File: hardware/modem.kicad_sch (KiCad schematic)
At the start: 30 parts, among them J11 PRPC001DAAN-RC, Q3 IRLML2246TRPBF, Q4 MMBT3904, U6 SN74AVC4T245PW, U7 SARA-R500S-61B

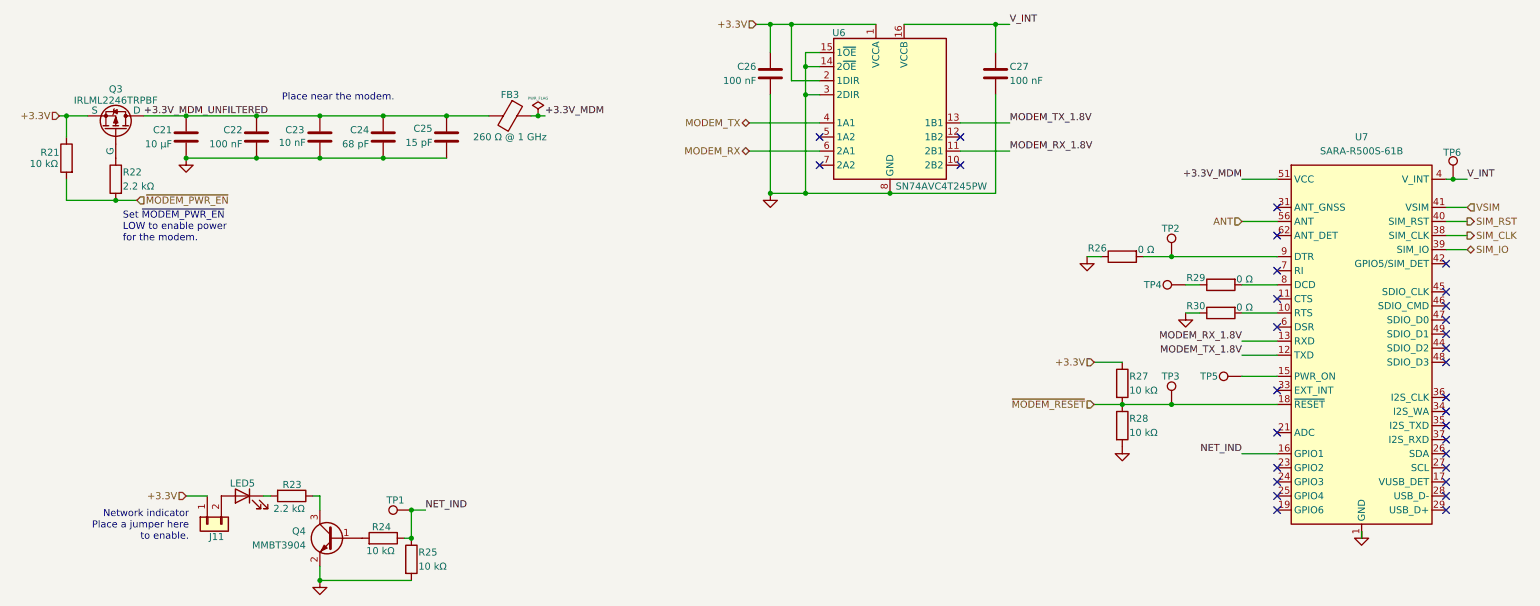
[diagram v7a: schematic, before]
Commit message: HW: Update VBAT, schema and layout
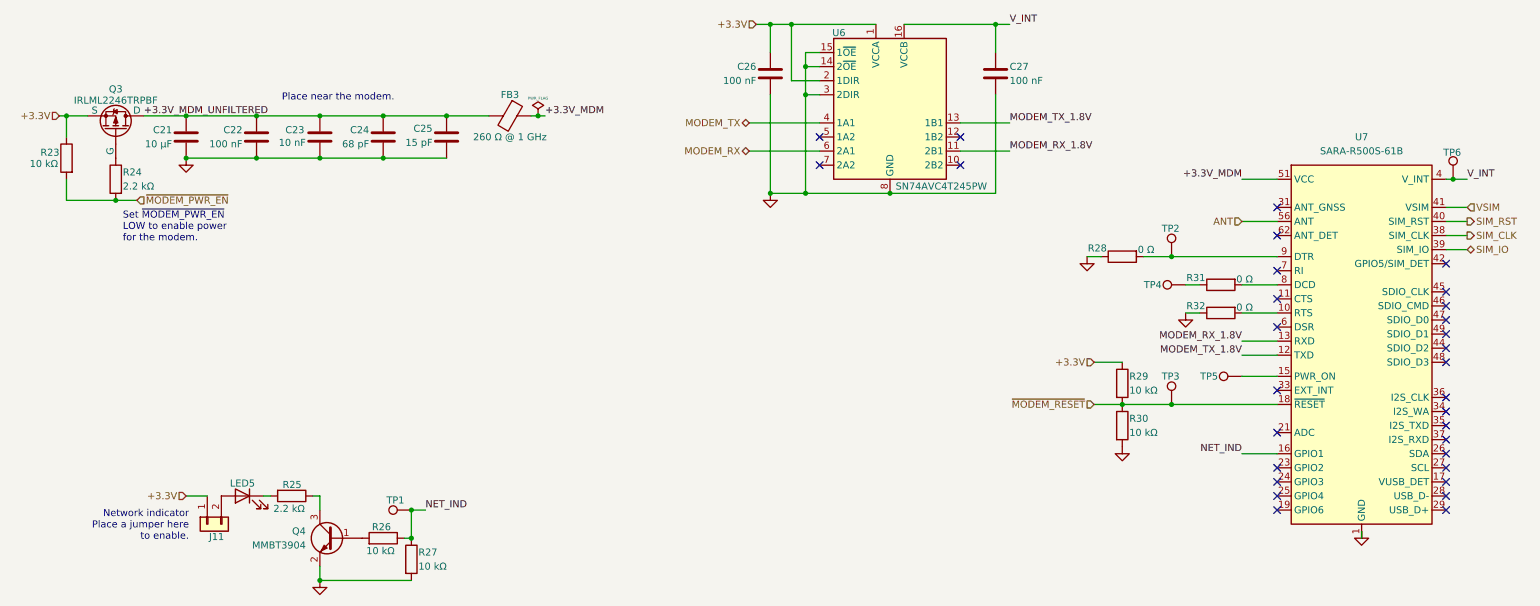
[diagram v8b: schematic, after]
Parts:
- renumbered R21 to R23, R22 to R24, R23 to R25, R24 to R26, R25 to R27, R26 to R28, R27 to R29, R28 to R30, R29 to R31, R30 to R32
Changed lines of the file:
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@@
 		(on_board yes)
 		(dnp no)
-		(property "Reference" "R27"
+		(property "Reference" "R29"
 			(at 213.36 134.62 0)
 			(effects
@@
 			(project "iida_devkit"
 				(path "/b12a6e25-97fb-4aba-bc96-af8db389bb9a/3723475b-e956-4027-ac40-e47346743900"
-					(reference "R27")
+					(reference "R29")
 					(unit 1)
 				)
@@
 		(on_board yes)
 		(dnp no)
-		(property "Reference" "R24"
+		(property "Reference" "R26"
 			(at 76.708 161.798 90)
 			(effects
@@
 			(project "iida_devkit"
 				(path "/b12a6e25-97fb-4aba-bc96-af8db389bb9a/3723475b-e956-4027-ac40-e47346743900"
-					(reference "R24")
+					(reference "R26")
 					(unit 1)
 				)
@@
 		(on_board yes)
 		(dnp no)
-		(property "Reference" "R28"
+		(property "Reference" "R30"
 			(at 213.36 142.24 0)
 			(effects
@@
 			(project "iida_devkit"
 				(path "/b12a6e25-97fb-4aba-bc96-af8db389bb9a/3723475b-e956-4027-ac40-e47346743900"
-					(reference "R28")
+					(reference "R30")
 					(unit 1)
 				)
@@
 		(on_board yes)
 		(dnp no)
-		(property "Reference" "R25"
+		(property "Reference" "R27"
 			(at 85.09 166.37 0)
 			(effects
@@
 			(project "iida_devkit"
 				(path "/b12a6e25-97fb-4aba-bc96-af8db389bb9a/3723475b-e956-4027-ac40-e47346743900"
-					(reference "R25")
+					(reference "R27")
 					(unit 1)
 				)
@@
 		(on_board yes)
 		(dnp no)
-		(property "Reference" "R21"
+		(property "Reference" "R23"
 			(at 20.32 94.234 0)
 			(effects
@@
 			(project "iida_devkit"
 				(path "/b12a6e25-97fb-4aba-bc96-af8db389bb9a/3723475b-e956-4027-ac40-e47346743900"
-					(reference "R21")
+					(reference "R23")
 					(unit 1)
 				)
@@
 		(on_board yes)
 		(dnp no)
-		(property "Reference" "R22"
+		(property "Reference" "R24"
 			(at 31.75 97.79 0)
 			(effects
@@
 			(project "iida_devkit"
 				(path "/b12a6e25-97fb-4aba-bc96-af8db389bb9a/3723475b-e956-4027-ac40-e47346743900"
-					(reference "R22")
+					(reference "R24")
 					(unit 1)
 				)
@@
 		(on_board yes)
 		(dnp no)
-		(property "Reference" "R30"
+		(property "Reference" "R32"
 			(at 227.076 121.92 90)
 			(effects
@@
 			(project "iida_devkit"
 				(path "/b12a6e25-97fb-4aba-bc96-af8db389bb9a/3723475b-e956-4027-ac40-e47346743900"
-					(reference "R30")
+					(reference "R32")
 					(unit 1)
 				)
@@
 		(on_board yes)
 		(dnp no)
-		(property "Reference" "R23"
+		(property "Reference" "R25"
 			(at 64.008 154.178 90)
 			(effects
@@
 			(project "iida_devkit"
 				(path "/b12a6e25-97fb-4aba-bc96-af8db389bb9a/3723475b-e956-4027-ac40-e47346743900"
-					(reference "R23")
+					(reference "R25")
 					(unit 1)
 				)
@@
 		(on_board yes)
 		(dnp no)
-		(property "Reference" "R26"
+		(property "Reference" "R28"
 			(at 209.296 111.506 90)
 			(effects
@@
 			(project "iida_devkit"
 				(path "/b12a6e25-97fb-4aba-bc96-af8db389bb9a/3723475b-e956-4027-ac40-e47346743900"
-					(reference "R26")
+					(reference "R28")
 					(unit 1)
 				)
@@
 		(on_board yes)
 		(dnp no)
-		(property "Reference" "R29"
+		(property "Reference" "R31"
 			(at 227.076 116.84 90)
 			(effects
@@
 			(project "iida_devkit"
 				(path "/b12a6e25-97fb-4aba-bc96-af8db389bb9a/3723475b-e956-4027-ac40-e47346743900"
-					(reference "R29")
+					(reference "R31")
 					(unit 1)
 				)
